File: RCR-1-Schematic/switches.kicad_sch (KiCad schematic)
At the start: 13 parts, among them M1 Minutes_Counter, SW2 Rst/Stop/Count Switch, SW3 CAL (Momentary), SW4 Ratemeter Scaler

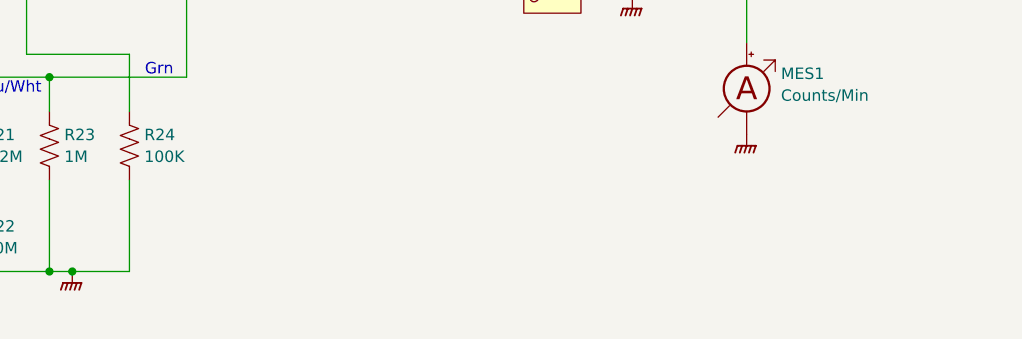
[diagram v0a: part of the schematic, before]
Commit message: Add some oscilloscope screenshots, fixed some mistakes
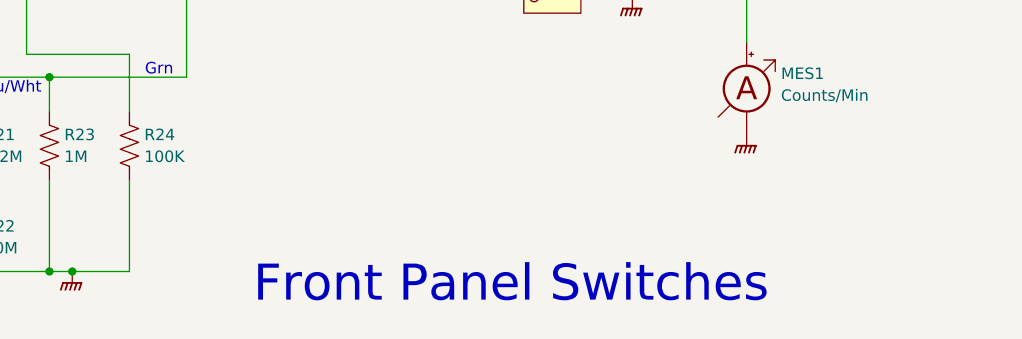
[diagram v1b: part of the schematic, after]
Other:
- note added: "Front Panel Switches"
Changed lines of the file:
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@@
+		)
+	)
+	(text "Front Panel Switches"
+		(exclude_from_sim no)
+		(at 151.638 138.684 0)
+		(effects
+			(font
+				(size 4 4)
+			)
 		)
 	)
